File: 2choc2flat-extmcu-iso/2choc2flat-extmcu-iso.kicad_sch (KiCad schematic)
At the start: 144 parts, among them J1 Conn_01x09_Male, J2 Conn_01x05_Male, J3 Conn_01x09_Male, K1 KEYSW, K10 KEYSW, K11 KEYSW, K12 KEYSW, K13 KEYSW, K14 KEYSW, K15 KEYSW, K16 KEYSW, K17 KEYSW, K18 KEYSW, K19 KEYSW, K2 KEYSW, K20 KEYSW, K21 KEYSW, K22 KEYSW, K23 KEYSW, K24 KEYSW, K25 KEYSW, K26 KEYSW, K27 KEYSW, K28 KEYSW, K29 KEYSW, K29-1 KEYSW, K3 KEYSW, K30 KEYSW, K31 KEYSW, K32 KEYSW, K33 KEYSW, K34 KEYSW, K35 KEYSW, K36 KEYSW, K37 KEYSW, K38 KEYSW, K39 KEYSW, K4 KEYSW, K40 KEYSW, K41 KEYSW, K42 KEYSW, K43 KEYSW, K44 KEYSW, K45 KEYSW, K46 KEYSW, K47 KEYSW, K48 KEYSW, K49 KEYSW, K5 KEYSW, K50 KEYSW, K51 KEYSW, K52 KEYSW, K53 KEYSW, K54 KEYSW, K55 KEYSW, K56 KEYSW, K57 KEYSW, K58 KEYSW, K59 KEYSW, K6 KEYSW, K60 KEYSW, K61 KEYSW, K62 KEYSW, K63 KEYSW, K64 KEYSW, K65 KEYSW, K7 KEYSW, K8 KEYSW, K9 KEYSW

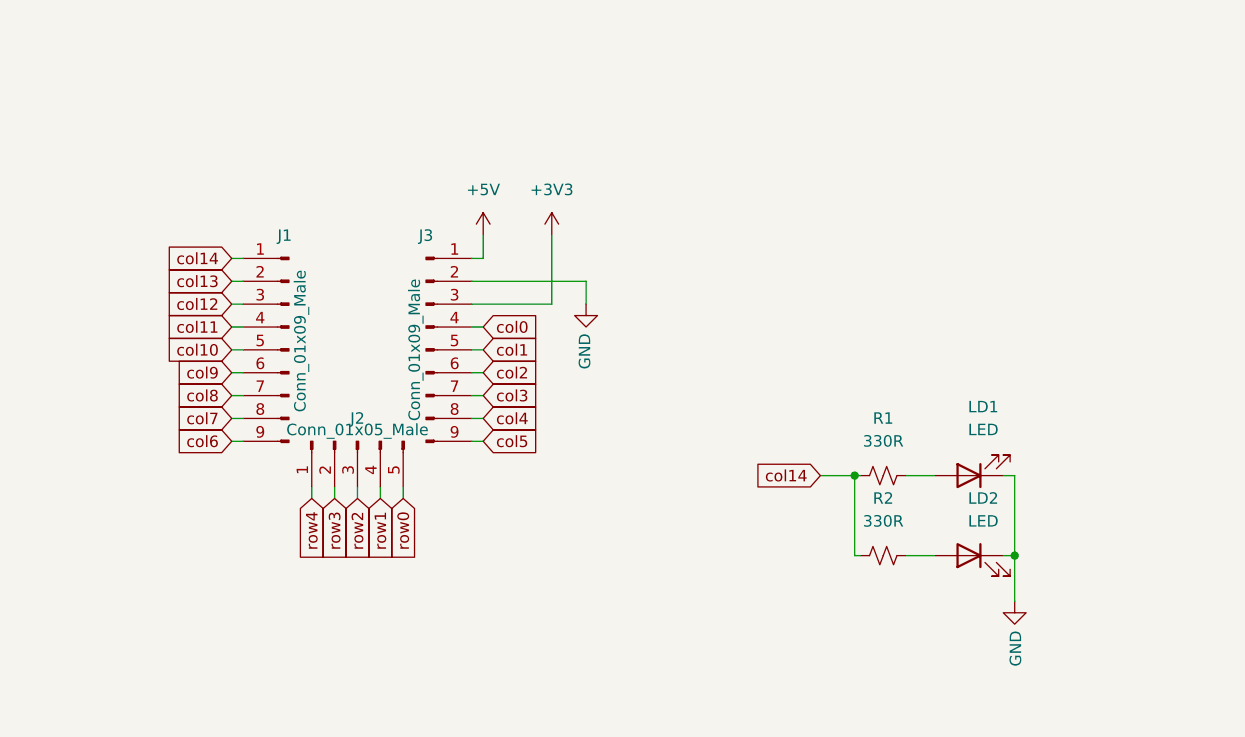
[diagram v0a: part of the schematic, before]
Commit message: revision 1.5 bothering to use the castellated pads
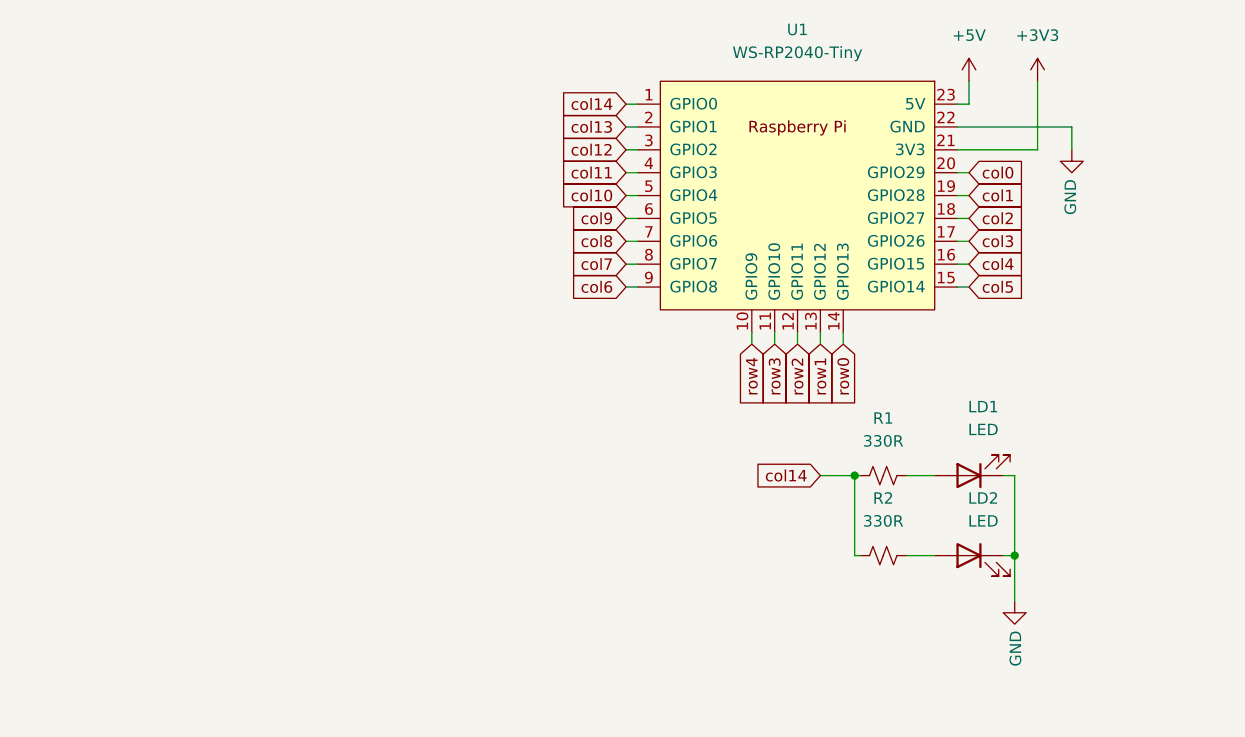
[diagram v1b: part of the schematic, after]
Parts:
- removed J1, J3: Conn_01x09_Male, Connector_PinHeader_2.54mm:PinHeader_1x09_P2.54mm_Vertical, symbol Connector:Conn_01x09_Male
- removed J2: Conn_01x05_Male, Connector_PinHeader_2.54mm:PinHeader_1x05_P2.54mm_Vertical, symbol Connector:Conn_01x05_Male
- added U1: WS-RP2040-Tiny, schizobovine:WAVESHARE_RP2040_TINY, symbol schizobovine:WS-RP2040-Tiny
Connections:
- net +3V3: now also U1.21 (3V3)
- net +5V: now also U1.23 (5V)
- net GND: now also U1.22 (GND)
- net col0: now also U1.20 (GPIO29)
- net col1: now also U1.19 (GPIO28)
- net col10: now also U1.5 (GPIO4)
- net col11: now also U1.4 (GPIO3)
- net col12: now also U1.3 (GPIO2)
- net col13: now also U1.2 (GPIO1)
- net col14: now also U1.1 (GPIO0)
- net col2: now also U1.18 (GPIO27)
- net col3: now also U1.17 (GPIO26)
- net col4: now also U1.16 (GPIO15)
- net col5: now also U1.15 (GPIO14)
- net col6: now also U1.9 (GPIO8)
- net col7: now also U1.8 (GPIO7)
- net col8: now also U1.7 (GPIO6)
- net col9: now also U1.6 (GPIO5)
- net row0: now also U1.14 (GPIO13)
- net row1: now also U1.13 (GPIO12)
- net row2: now also U1.12 (GPIO11)
- net row3: now also U1.11 (GPIO10)
- net row4: now also U1.10 (GPIO9)

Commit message: wip adding RGB lighting
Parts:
- removed K29-1: KEYSW, Switch_Keyboard_Hotswap_Kailh_mine:SW_Hotswap_Kailh_Choc_V2_1.25u, symbol keyboard_parts:KEYSW
- removed LD1, LD2: LED, schizobovine:LED_1206_3216Metric_ReverseMount_Hole1.8x2.4mm, symbol Device:LED
- removed R1, R2: 330R, schizobovine:R_0603_1608Metric, symbol Device:R_Small_US
- added LD1, LD10, LD11, LD12, LD13, LD14, LD15, LD16, LD17, LD18, LD19, LD2, LD20, LD21, LD22, LD23, LD24, LD25, LD26, LD27, LD28, LD29, LD3, LD30, LD31, LD32, LD33, LD34, LD35, LD36, LD37, LD38, LD39, LD4, LD40, LD41, LD42, LD43, LD44, LD45, LD46, LD47, LD48, LD49, LD5, LD50, LD51, LD52, LD53, LD54, LD55, LD56, LD57, LD58, LD59, LD6, LD60, LD61, LD62, LD63, LD64, LD65, LD7, LD8, LD9: SK6812MINI, schizobovine:LED_SK6812MINI_PLCC4_3.5x2.8mm_P1.75mm_reverse_mount, symbol schizobovine:SK6812MINI
- K42: footprint Switch_Keyboard_Hotswap_Kailh_mine:SW_Hotswap_Kailh_Choc_V2_ISOEnter_West_Gateron_LP_Stabs -> Switch_Keyboard_Hotswap_Kailh_mine:SW_Hotswap_Kailh_Choc_V2_ISOEnter_180deg_West_Gateron_LP_Stabs
- K43: footprint Switch_Keyboard_Hotswap_Kailh_mine:SW_Hotswap_Kailh_Choc_V2_2.00u_90deg_Gateron_LP_Stabs -> Switch_Keyboard_Hotswap_Kailh_mine:SW_Hotswap_Kailh_Choc_V2_2.00u_270deg_Gateron_LP_Stabs
- U1: footprint schizobovine:WAVESHARE_RP2040_TINY -> schizobovine:WAVESHARE_RP2040_TINY_SLIM
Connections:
- net +5V: now also LD1.4 (VDD), LD10.4 (VDD), LD11.4 (VDD), LD12.4 (VDD), LD13.4 (VDD), LD14.4 (VDD), LD15.4 (VDD), LD16.4 (VDD), LD17.4 (VDD), LD18.4 (VDD), LD19.4 (VDD), LD2.4 (VDD), LD20.4 (VDD), LD21.4 (VDD), LD22.4 (VDD), LD23.4 (VDD), LD24.4 (VDD), LD25.4 (VDD), LD26.4 (VDD), LD27.4 (VDD), LD28.4 (VDD), LD29.4 (VDD), LD3.4 (VDD), LD30.4 (VDD), LD31.4 (VDD), LD32.4 (VDD), LD33.4 (VDD), LD34.4 (VDD), LD35.4 (VDD), LD36.4 (VDD), LD37.4 (VDD), LD38.4 (VDD), LD39.4 (VDD), LD4.4 (VDD), LD40.4 (VDD), LD41.4 (VDD), LD42.4 (VDD), LD43.4 (VDD), LD44.4 (VDD), LD45.4 (VDD), LD46.4 (VDD), LD47.4 (VDD), LD48.4 (VDD), LD49.4 (VDD), LD5.4 (VDD), LD50.4 (VDD), LD51.4 (VDD), LD52.4 (VDD), LD53.4 (VDD), LD54.4 (VDD), LD55.4 (VDD), LD56.4 (VDD), LD57.4 (VDD), LD58.4 (VDD), LD59.4 (VDD), LD6.4 (VDD), LD60.4 (VDD), LD61.4 (VDD), LD62.4 (VDD), LD63.4 (VDD), LD64.4 (VDD), LD65.4 (VDD), LD7.4 (VDD), LD8.4 (VDD), LD9.4 (VDD)
- net GND: now also LD1.2 (VSS), LD10.2 (VSS), LD11.2 (VSS), LD12.2 (VSS), LD13.2 (VSS), LD14.2 (VSS), LD15.2 (VSS), LD16.2 (VSS), LD17.2 (VSS), LD18.2 (VSS), LD19.2 (VSS), LD2.2 (VSS), LD20.2 (VSS), LD21.2 (VSS), LD22.2 (VSS), LD23.2 (VSS), LD24.2 (VSS), LD25.2 (VSS), LD26.2 (VSS), LD27.2 (VSS), LD28.2 (VSS), LD29.2 (VSS), LD3.2 (VSS), LD30.2 (VSS), LD31.2 (VSS), LD32.2 (VSS), LD33.2 (VSS), LD34.2 (VSS), LD35.2 (VSS), LD36.2 (VSS), LD37.2 (VSS), LD38.2 (VSS), LD39.2 (VSS), LD4.2 (VSS), LD40.2 (VSS), LD41.2 (VSS), LD42.2 (VSS), LD43.2 (VSS), LD44.2 (VSS), LD45.2 (VSS), LD46.2 (VSS), LD47.2 (VSS), LD48.2 (VSS), LD49.2 (VSS), LD5.2 (VSS), LD50.2 (VSS), LD51.2 (VSS), LD52.2 (VSS), LD53.2 (VSS), LD54.2 (VSS), LD55.2 (VSS), LD56.2 (VSS), LD57.2 (VSS), LD58.2 (VSS), LD59.2 (VSS), LD6.2 (VSS), LD60.2 (VSS), LD61.2 (VSS), LD62.2 (VSS), LD63.2 (VSS), LD64.2 (VSS), LD65.2 (VSS), LD7.2 (VSS), LD8.2 (VSS), LD9.2 (VSS)
- net col0: now also K17.1, K2.1, K29.1, K30.1, K44.1, K58.1; no longer K29.2
- net col1: now also K18.1, K19.1, K3.1, K31.1, K32.1, K4.1, K45.1, K46.1, K59.1; no longer K17.1, K2.1, K30.1, K44.1, K58.1
- net col2: now also K20.1, K21.1, K33.1, K34.1, K47.1, K48.1, K5.1, K6.1; no longer K18.1, K3.1, K31.1, K45.1, K59.1
- net col3: now also K22.1, K23.1, K35.1, K36.1, K49.1, K50.1, K60.1, K7.1, K8.1; no longer K19.1, K32.1, K4.1, K46.1
- net col4: now also K10.1, K24.1, K25.1, K37.1, K38.1, K51.1, K52.1, K61.1, K9.1; no longer K20.1, K33.1, K47.1, K5.1
- net col5: now also K11.1, K12.1, K26.1, K27.1, K39.1, K40.1, K53.1, K54.1, K62.1, K63.1; no longer K21.1, K34.1, K48.1, K6.1
- net col6: now also K13.1, K14.1, K15.1, K28.1, K41.1, K42.1, K55.1, K56.1, K64.1, K65.1, U1.14 (GPIO13); no longer K22.1, K35.1, K49.1, K60.1, K7.1, U1.9 (GPIO8)
- net row0: now also U1.13 (GPIO12); no longer D10.1 (K), D12.1 (K), D14.1 (K), D2.1 (K), D4.1 (K), D6.1 (K), D8.1 (K), U1.14 (GPIO13)
- net row1: now also D10.1 (K), D12.1 (K), D14.1 (K), D2.1 (K), D4.1 (K), D6.1 (K), D8.1 (K), U1.12 (GPIO11); no longer D15.1 (K), D16.1 (K), D17.1 (K), D18.1 (K), D19.1 (K), D20.1 (K), D21.1 (K), D22.1 (K), D23.1 (K), D24.1 (K), D25.1 (K), D26.1 (K), D27.1 (K), D28.1 (K), U1.13 (GPIO12)
- net row2: now also D16.1 (K), D18.1 (K), D20.1 (K), D22.1 (K), D24.1 (K), D26.1 (K), D28.1 (K), U1.11 (GPIO10); no longer D29.1 (K), D30.1 (K), D31.1 (K), D32.1 (K), D33.1 (K), D34.1 (K), D35.1 (K), D36.1 (K), D37.1 (K), D38.1 (K), D39.1 (K), D40.1 (K), D41.1 (K), D42.1 (K), U1.12 (GPIO11)
- net row3: now also D15.1 (K), D17.1 (K), D19.1 (K), D21.1 (K), D23.1 (K), D25.1 (K), D27.1 (K), U1.10 (GPIO9); no longer D43.1 (K), D44.1 (K), D45.1 (K), D46.1 (K), D47.1 (K), D48.1 (K), D49.1 (K), D50.1 (K), D51.1 (K), D52.1 (K), D53.1 (K), D54.1 (K), D55.1 (K), D56.1 (K), U1.11 (GPIO10)
- net row4: now also D29.1 (K), D31.1 (K), D33.1 (K), D35.1 (K), D37.1 (K), D39.1 (K), D41.1 (K), U1.9 (GPIO8); no longer D57.1 (K), D58.1 (K), D59.1 (K), D60.1 (K), D61.1 (K), D62.1 (K), D63.1 (K), D64.1 (K), D65.1 (K), U1.10 (GPIO9)
- net at D29.2 (A): now also K29.2; no longer K29.1
- net at D42.2 (A): now also K42.2; no longer K42.1
- removed net col10: K11.1, K26.1, K39.1, K53.1, K62.1, U1.5 (GPIO4)
- removed net col11: K12.1, K27.1, K40.1, K54.1, K63.1, U1.4 (GPIO3)
- removed net col12: K13.1, K28.1, K41.1, K55.1, K64.1, U1.3 (GPIO2)
- removed net col13: K14.1, K15.1, K42.2, K56.1, K65.1, U1.2 (GPIO1)
- net col14 renamed caps
- removed net col7: K23.1, K36.1, K50.1, K8.1, U1.8 (GPIO7)
- removed net col8: K24.1, K37.1, K51.1, K9.1, U1.7 (GPIO6)
- removed net col9: K10.1, K25.1, K38.1, K52.1, K61.1, U1.6 (GPIO5)
- new net: LD34.1 (DOUT), LD35.3 (DIN)
- new net: LD33.1 (DOUT), LD34.3 (DIN)
- new net: LD12.1 (DOUT), LD13.3 (DIN)
- new net: LD11.1 (DOUT), LD12.3 (DIN)
- new net: LD6.1 (DOUT), LD7.3 (DIN)
- new net: LD5.1 (DOUT), LD6.3 (DIN)
- new net: LD36.1 (DOUT), LD37.3 (DIN)
- new net: LD35.1 (DOUT), LD36.3 (DIN)
- new net: LD3.1 (DOUT), LD4.3 (DIN)
- new net: LD2.1 (DOUT), LD3.3 (DIN)
- new net: LD62.1 (DOUT), LD63.3 (DIN)
- new net: LD61.1 (DOUT), LD62.3 (DIN)
- new net: LD59.1 (DOUT), LD60.3 (DIN)
- new net: LD58.1 (DOUT), LD59.3 (DIN)
- new net: LD40.1 (DOUT), LD41.3 (DIN)
- new net: LD39.1 (DOUT), LD40.3 (DIN)
- new net: LD4.1 (DOUT), LD5.3 (DIN)
- new net: LD28.1 (DOUT), LD29.3 (DIN)
- new net: LD27.1 (DOUT), LD28.3 (DIN)
- new net: LD56.1 (DOUT), LD57.3 (DIN)
- new net: LD55.1 (DOUT), LD56.3 (DIN)
- new net: LD54.1 (DOUT), LD55.3 (DIN)
- new net: LD53.1 (DOUT), LD54.3 (DIN)
- new net: LD37.1 (DOUT), LD38.3 (DIN)
- new net: LD26.1 (DOUT), LD27.3 (DIN)
- new net: LD25.1 (DOUT), LD26.3 (DIN)
- new net: LD21.1 (DOUT), LD22.3 (DIN)
- new net: LD20.1 (DOUT), LD21.3 (DIN)
- new net: LD46.1 (DOUT), LD47.3 (DIN)
- new net: LD45.1 (DOUT), LD46.3 (DIN)
- new net: LD19.1 (DOUT), LD20.3 (DIN)
- new net: LD18.1 (DOUT), LD19.3 (DIN)
- new net: LD1.1 (DOUT), LD2.3 (DIN)
- new net: LD23.1 (DOUT), LD24.3 (DIN)
- new net: LD22.1 (DOUT), LD23.3 (DIN)
- new net: LD7.1 (DOUT), LD8.3 (DIN)
- new net: LD17.1 (DOUT), LD18.3 (DIN)
- new net: LD31.1 (DOUT), LD32.3 (DIN)
- new net: LD30.1 (DOUT), LD31.3 (DIN)
- new net: LD64.1 (DOUT), LD65.3 (DIN)
- new net: LD63.1 (DOUT), LD64.3 (DIN)
- new net: LD13.1 (DOUT), LD14.3 (DIN)
- new net: LD47.1 (DOUT), LD48.3 (DIN)
- new net: LD24.1 (DOUT), LD25.3 (DIN)
- new net: LD52.1 (DOUT), LD53.3 (DIN)
- new net: LD51.1 (DOUT), LD52.3 (DIN)
- new net: LD8.1 (DOUT), LD9.3 (DIN)
- new net: LD29.1 (DOUT), LD30.3 (DIN)
- new net: LD57.1 (DOUT), LD58.3 (DIN)
- new net: LD44.1 (DOUT), LD45.3 (DIN)
- new net: LD43.1 (DOUT), LD44.3 (DIN)
- new net: LD10.1 (DOUT), LD11.3 (DIN)
- new net: LD10.3 (DIN), LD9.1 (DOUT)
- new net: LD16.1 (DOUT), LD17.3 (DIN)
- new net: LD50.1 (DOUT), LD51.3 (DIN)
- new net: LD60.1 (DOUT), LD61.3 (DIN)
- new net: LD42.1 (DOUT), LD43.3 (DIN)
- new net: LD41.1 (DOUT), LD42.3 (DIN)
- new net: LD49.1 (DOUT), LD50.3 (DIN)
- new net: LD38.1 (DOUT), LD39.3 (DIN)
- new net: LD32.1 (DOUT), LD33.3 (DIN)
- new net: LD15.1 (DOUT), LD16.3 (DIN)
- new net: LD14.1 (DOUT), LD15.3 (DIN)
- new net backlight: LD1.3 (DIN), U1.2 (GPIO1)
- new net row5: D30.1 (K), D32.1 (K), D34.1 (K), D36.1 (K), D38.1 (K), D40.1 (K), D42.1 (K), U1.8 (GPIO7)
- new net row6: D43.1 (K), D45.1 (K), D47.1 (K), D49.1 (K), D51.1 (K), D53.1 (K), D55.1 (K), U1.7 (GPIO6)
- new net row7: D44.1 (K), D46.1 (K), D48.1 (K), D50.1 (K), D52.1 (K), D54.1 (K), D56.1 (K), U1.6 (GPIO5)
- new net row8: D57.1 (K), D59.1 (K), D60.1 (K), D61.1 (K), D62.1 (K), D64.1 (K), U1.5 (GPIO4)
- new net row9: D58.1 (K), D63.1 (K), D65.1 (K), U1.4 (GPIO3)
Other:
- moved on the sheet: D1, D10, D11, D12, D13, D14, D15, D16, D17, D18, D19, D2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

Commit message: wip adding lighting
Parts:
- added R1: 100R, schizobovine:C_0603_1608Metric, symbol Device:R_Small_US
- added U2: 74LVC1G125, Package_TO_SOT_SMD:SOT-23-5_HandSoldering, symbol 74xGxx:74LVC1G125
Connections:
- net caps is gone; now on net backlight: U1.1 (GPIO0)
- net +5V: now also U2.5 (VCC)
- net GND: now also U2.1, U2.3 (GND)
- net backlight: now also R1.1; no longer LD1.3 (DIN), U1.2 (GPIO1)
- net at LD48.1 (DOUT): now also LD49.3 (DIN)
- new net: R1.2, U2.2
- new net backlight_5v: LD1.3 (DIN), U2.4

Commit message: version 2.0 with RGB backlighting and underglow
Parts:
- removed R1: 100R, schizobovine:C_0603_1608Metric, symbol Device:R_Small_US
- removed U2: 74LVC1G125, Package_TO_SOT_SMD:SOT-23-5_HandSoldering, symbol 74xGxx:74LVC1G125
- added BD1, BD10, BD11, BD12, BD13, BD14, BD15, BD16, BD2, BD3, BD4, BD5, BD6, BD7, BD8, BD9: WS2812B, schizobovine:LED_WS2812B_NANO_2020, symbol LED:WS2812B
- added C1: 1u, schizobovine:C_0603_1608Metric, symbol Device:C_Small
- added U2: 74LVC2G125, Package_SO:SSOP-8_2.95x2.8mm_P0.65mm, symbol 74xGxx:74LVC2G125
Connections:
- net +5V: now also BD1.1 (VDD), BD10.1 (VDD), BD11.1 (VDD), BD12.1 (VDD), BD13.1 (VDD), BD14.1 (VDD), BD15.1 (VDD), BD16.1 (VDD), BD2.1 (VDD), BD3.1 (VDD), BD4.1 (VDD), BD5.1 (VDD), BD6.1 (VDD), BD7.1 (VDD), BD8.1 (VDD), BD9.1 (VDD), C1.1, U2.8 (VCC), U2.8 (VCC)
- net GND: now also BD1.3 (VSS), BD10.3 (VSS), BD11.3 (VSS), BD12.3 (VSS), BD13.3 (VSS), BD14.3 (VSS), BD15.3 (VSS), BD16.3 (VSS), BD2.3 (VSS), BD3.3 (VSS), BD4.3 (VSS), BD5.3 (VSS), BD6.3 (VSS), BD7.3 (VSS), BD8.3 (VSS), BD9.3 (VSS), C1.2, U2.1, U2.4 (GND), U2.4 (GND), U2.7
- net at LD28.1 (DOUT): now also LD27.3 (DIN); no longer LD29.3 (DIN)
- net at LD28.3 (DIN): now also LD15.1 (DOUT); no longer LD27.1 (DOUT)
- net at LD56.1 (DOUT): now also LD55.3 (DIN); no longer LD57.3 (DIN)
- net at LD56.3 (DIN): now also LD42.1 (DOUT); no longer LD55.1 (DOUT)
- net at LD54.1 (DOUT): now also LD53.3 (DIN); no longer LD55.3 (DIN)
- net at LD54.3 (DIN): now also LD55.1 (DOUT); no longer LD53.1 (DOUT)
- net at LD26.1 (DOUT): now also LD25.3 (DIN); no longer LD27.3 (DIN)
- net at LD26.3 (DIN): now also LD27.1 (DOUT); no longer LD25.1 (DOUT)
- net at LD21.1 (DOUT): now also LD20.3 (DIN); no longer LD22.3 (DIN)
- net at LD21.3 (DIN): now also LD22.1 (DOUT); no longer LD20.1 (DOUT)
- net at LD46.1 (DOUT): now also LD45.3 (DIN); no longer LD47.3 (DIN)
- net at LD46.3 (DIN): now also LD47.1 (DOUT); no longer LD45.1 (DOUT)
- net at LD19.1 (DOUT): now also LD18.3 (DIN); no longer LD20.3 (DIN)
- net at LD19.3 (DIN): now also LD20.1 (DOUT); no longer LD18.1 (DOUT)
- net at LD23.1 (DOUT): now also LD22.3 (DIN); no longer LD24.3 (DIN)
- net at LD23.3 (DIN): now also LD24.1 (DOUT); no longer LD22.1 (DOUT)
- net at LD17.1 (DOUT): now also LD16.3 (DIN); no longer LD18.3 (DIN)
- net at LD48.3 (DIN): now also LD49.1 (DOUT); no longer LD47.1 (DOUT)
- net at LD52.1 (DOUT): now also LD51.3 (DIN); no longer LD53.3 (DIN)
- net at LD52.3 (DIN): now also LD53.1 (DOUT); no longer LD51.1 (DOUT)
- net at LD48.1 (DOUT): now also LD47.3 (DIN); no longer LD49.3 (DIN)
- net at LD44.1 (DOUT): now also LD43.3 (DIN); no longer LD45.3 (DIN)
- net at LD44.3 (DIN): now also LD45.1 (DOUT); no longer LD43.1 (DOUT)
- net at LD17.3 (DIN): now also LD18.1 (DOUT); no longer LD16.1 (DOUT)
- net at LD50.1 (DOUT): now also LD49.3 (DIN); no longer LD51.3 (DIN)
- net at LD50.3 (DIN): now also LD51.1 (DOUT); no longer LD49.1 (DOUT)
- net underglow: now reaches U1.2 (GPIO1)
- net underglow: now also U2.2
- net backlight renamed per_key_rgb
- net per_key_rgb: now also U2.5
- net backlight_5v renamed per_key_rgb_5v
- net per_key_rgb_5v: now also U2.3
- new net: BD2.2 (DOUT), BD3.4 (DIN)
- new net: BD1.2 (DOUT), BD2.4 (DIN)
- new net: BD11.2 (DOUT), BD12.4 (DIN)
- new net: BD10.2 (DOUT), BD11.4 (DIN)
- new net: BD15.2 (DOUT), BD16.4 (DIN)
- new net: BD10.4 (DIN), BD9.2 (DOUT)
- new net: BD8.2 (DOUT), BD9.4 (DIN)
- new net: BD5.2 (DOUT), BD6.4 (DIN)
- new net: BD4.2 (DOUT), BD5.4 (DIN)
- new net: BD13.2 (DOUT), BD14.4 (DIN)
- new net: BD12.2 (DOUT), BD13.4 (DIN)
- new net: BD14.2 (DOUT), BD15.4 (DIN)
- new net: BD6.2 (DOUT), BD7.4 (DIN)
- new net: LD24.3 (DIN), LD25.1 (DOUT)
- new net: BD3.2 (DOUT), BD4.4 (DIN)
- new net: LD43.1 (DOUT), LD57.3 (DIN)
- new net: LD16.1 (DOUT), LD29.3 (DIN)
- new net: BD7.2 (DOUT), BD8.4 (DIN)
- new net underglow_5v: BD1.4 (DIN), U2.6
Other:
- moved on the sheet: LD1, LD10, LD11, LD12, LD13, LD14, LD15, LD16, LD17, LD18, LD19, LD2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

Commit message: v2.1 few LEDs out of alignment
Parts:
- K60: footprint Switch_Keyboard_Hotswap_Kailh_mine:SW_Hotswap_Kailh_Choc_V2_6.25u -> Switch_Keyboard_Hotswap_Kailh_mine:SW_Hotswap_Kailh_Choc_V2_6.25u_special
- LD1, LD10, LD11, LD12, LD13, LD14, LD15, LD16, LD17, LD18, LD19, LD2, LD20, LD21, LD22, LD23, LD24, LD25, LD26, LD27, LD28, LD29, LD3, LD30, LD31, LD32, LD33, LD34, LD35, LD36, LD37, LD38, LD39, LD4, LD40, LD41, LD42, LD43, LD44, LD45, LD46, LD47, LD48, LD49, LD5, LD50, LD51, LD52, LD53, LD54, LD55, LD56, LD57, LD58, LD59, LD6, LD60, LD61, LD62, LD63, LD64, LD65, LD7, LD8, LD9: footprint schizobovine:LED_SK6812MINI_PLCC4_3.5x2.8mm_P1.75mm_reverse_mount -> schizobovine:LED_SK6812MINI_PLCC4_3.1x2.7mm_P1.75mm_reverse_mount

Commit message: restore non-RGB versions from history into separate dirs
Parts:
- removed BD1, BD10, BD11, BD12, BD13, BD14, BD15, BD16, BD2, BD3, BD4, BD5, BD6, BD7, BD8, BD9: WS2812B, schizobovine:LED_WS2812B_NANO_2020, symbol LED:WS2812B
- removed C1: 1u, schizobovine:C_0603_1608Metric, symbol Device:C_Small
- removed LD1, LD10, LD11, LD12, LD13, LD14, LD15, LD16, LD17, LD18, LD19, LD2, LD20, LD21, LD22, LD23, LD24, LD25, LD26, LD27, LD28, LD29, LD3, LD30, LD31, LD32, LD33, LD34, LD35, LD36, LD37, LD38, LD39, LD4, LD40, LD41, LD42, LD43, LD44, LD45, LD46, LD47, LD48, LD49, LD5, LD50, LD51, LD52, LD53, LD54, LD55, LD56, LD57, LD58, LD59, LD6, LD60, LD61, LD62, LD63, LD64, LD65, LD7, LD8, LD9: SK6812MINI, schizobovine:LED_SK6812MINI_PLCC4_3.1x2.7mm_P1.75mm_reverse_mount, symbol schizobovine:SK6812MINI
- removed U2: 74LVC2G125, Package_SO:SSOP-8_2.95x2.8mm_P0.65mm, symbol 74xGxx:74LVC2G125
- added K29-1: KEYSW, Switch_Keyboard_Hotswap_Kailh_mine:SW_Hotswap_Kailh_Choc_V2_1.25u, symbol keyboard_parts:KEYSW
- added LD1, LD2: LED, schizobovine:LED_1206_3216Metric_ReverseMount_Hole1.8x2.4mm, symbol Device:LED
- added R1, R2: 330R, schizobovine:R_0603_1608Metric, symbol Device:R_Small_US
- K42: footprint Switch_Keyboard_Hotswap_Kailh_mine:SW_Hotswap_Kailh_Choc_V2_ISOEnter_180deg_West_Gateron_LP_Stabs -> Switch_Keyboard_Hotswap_Kailh_mine:SW_Hotswap_Kailh_Choc_V2_ISOEnter_West_Gateron_LP_Stabs
- K43: footprint Switch_Keyboard_Hotswap_Kailh_mine:SW_Hotswap_Kailh_Choc_V2_2.00u_270deg_Gateron_LP_Stabs -> Switch_Keyboard_Hotswap_Kailh_mine:SW_Hotswap_Kailh_Choc_V2_2.00u_90deg_Gateron_LP_Stabs
- K60: footprint Switch_Keyboard_Hotswap_Kailh_mine:SW_Hotswap_Kailh_Choc_V2_6.25u_special -> Switch_Keyboard_Hotswap_Kailh_mine:SW_Hotswap_Kailh_Choc_V2_6.25u
- U1: footprint schizobovine:WAVESHARE_RP2040_TINY_SLIM -> schizobovine:WAVESHARE_RP2040_TINY
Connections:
- net GND: now also LD1.1 (K), LD2.1 (K)
- net col0: now also K29.2, K29-1.1; no longer K17.1, K2.1, K29.1, K30.1, K44.1, K58.1
- net col1: now also K17.1, K2.1, K30.1, K44.1, K58.1; no longer K18.1, K19.1, K3.1, K31.1, K32.1, K4.1, K45.1, K46.1, K59.1
- net col2: now also K18.1, K3.1, K31.1, K45.1, K59.1; no longer K20.1, K21.1, K33.1, K34.1, K47.1, K48.1, K5.1, K6.1
- net col3: now also K19.1, K32.1, K4.1, K46.1; no longer K22.1, K23.1, K35.1, K36.1, K49.1, K50.1, K60.1, K7.1, K8.1
- net col4: now also K20.1, K33.1, K47.1, K5.1; no longer K10.1, K24.1, K25.1, K37.1, K38.1, K51.1, K52.1, K61.1, K9.1
- net col5: now also K21.1, K34.1, K48.1, K6.1; no longer K11.1, K12.1, K26.1, K27.1, K39.1, K40.1, K53.1, K54.1, K62.1, K63.1
- net col6: now also K22.1, K35.1, K49.1, K60.1, K7.1, U1.9 (GPIO8); no longer K13.1, K14.1, K15.1, K28.1, K41.1, K42.1, K55.1, K56.1, K64.1, K65.1, U1.14 (GPIO13)
- net row0: now also D10.1 (K), D12.1 (K), D14.1 (K), D2.1 (K), D4.1 (K), D6.1 (K), D8.1 (K), U1.14 (GPIO13); no longer U1.13 (GPIO12)
- net row1: now also D15.1 (K), D16.1 (K), D17.1 (K), D18.1 (K), D19.1 (K), D20.1 (K), D21.1 (K), D22.1 (K), D23.1 (K), D24.1 (K), D25.1 (K), D26.1 (K), D27.1 (K), D28.1 (K), U1.13 (GPIO12); no longer D10.1 (K), D12.1 (K), D14.1 (K), D2.1 (K), D4.1 (K), D6.1 (K), D8.1 (K), U1.12 (GPIO11)
- net row2: now also D29.1 (K), D30.1 (K), D31.1 (K), D32.1 (K), D33.1 (K), D34.1 (K), D35.1 (K), D36.1 (K), D37.1 (K), D38.1 (K), D39.1 (K), D40.1 (K), D41.1 (K), D42.1 (K), U1.12 (GPIO11); no longer D16.1 (K), D18.1 (K), D20.1 (K), D22.1 (K), D24.1 (K), D26.1 (K), D28.1 (K), U1.11 (GPIO10)
- net row3: now also D43.1 (K), D44.1 (K), D45.1 (K), D46.1 (K), D47.1 (K), D48.1 (K), D49.1 (K), D50.1 (K), D51.1 (K), D52.1 (K), D53.1 (K), D54.1 (K), D55.1 (K), D56.1 (K), U1.11 (GPIO10); no longer D15.1 (K), D17.1 (K), D19.1 (K), D21.1 (K), D23.1 (K), D25.1 (K), D27.1 (K), U1.10 (GPIO9)
- net row4: now also D57.1 (K), D58.1 (K), D59.1 (K), D60.1 (K), D61.1 (K), D62.1 (K), D63.1 (K), D64.1 (K), D65.1 (K), U1.10 (GPIO9); no longer D29.1 (K), D31.1 (K), D33.1 (K), D35.1 (K), D37.1 (K), D39.1 (K), D41.1 (K), U1.9 (GPIO8)
- net at D29.2 (A): now also K29.1, K29-1.2; no longer K29.2
- net at D42.2 (A): now also K42.1; no longer K42.2
- net col12: now reaches U1.3 (GPIO2)
- net col12: now also K13.1, K28.1, K41.1, K55.1, K64.1
- net per_key_rgb renamed col14
- net col14: now also R1.1, R2.1
- removed net row5: D30.1 (K), D32.1 (K), D34.1 (K), D36.1 (K), D38.1 (K), D40.1 (K), D42.1 (K), U1.8 (GPIO7)
- removed net row6: D43.1 (K), D45.1 (K), D47.1 (K), D49.1 (K), D51.1 (K), D53.1 (K), D55.1 (K), U1.7 (GPIO6)
- removed net row7: D44.1 (K), D46.1 (K), D48.1 (K), D50.1 (K), D52.1 (K), D54.1 (K), D56.1 (K), U1.6 (GPIO5)
- removed net row8: D57.1 (K), D59.1 (K), D60.1 (K), D61.1 (K), D62.1 (K), D64.1 (K), U1.5 (GPIO4)
- removed net row9: D58.1 (K), D63.1 (K), D65.1 (K), U1.4 (GPIO3)
- net underglow renamed col13
- net col13: now also K14.1, K15.1, K42.2, K56.1, K65.1
- new net: LD1.2 (A), R1.2
- new net: LD2.2 (A), R2.2
- new net col10: K11.1, K26.1, K39.1, K53.1, K62.1, U1.5 (GPIO4)
- new net col11: K12.1, K27.1, K40.1, K54.1, K63.1, U1.4 (GPIO3)
- new net col7: K23.1, K36.1, K50.1, K8.1, U1.8 (GPIO7)
- new net col8: K24.1, K37.1, K51.1, K9.1, U1.7 (GPIO6)
- new net col9: K10.1, K25.1, K38.1, K52.1, K61.1, U1.6 (GPIO5)
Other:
- moved on the sheet: D1, D10, D11, D12, D13, D14, D15, D16, D17, D18, D19, D2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
